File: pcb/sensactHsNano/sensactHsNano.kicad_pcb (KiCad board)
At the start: 2 copper layers, 90 x 58.5 mm, 130 parts, among them J1 PROG, J2 SensactBus, J3 CAN+24V, J4 HR911105A, J5 Audio, J6 1wire, Q1 BC817, SW1 TERM, SW2 Prog, SW3 Reset, U1 TAS5805M, U10 HT75xx-1-SOT89, U2 LAN8720A, U3 ESP32, U4 DS2482, U5 SN65HVD230, U6 EL817, U7 TPS5430DDA, U8 EL817, U9 LM393, X1 50MHz

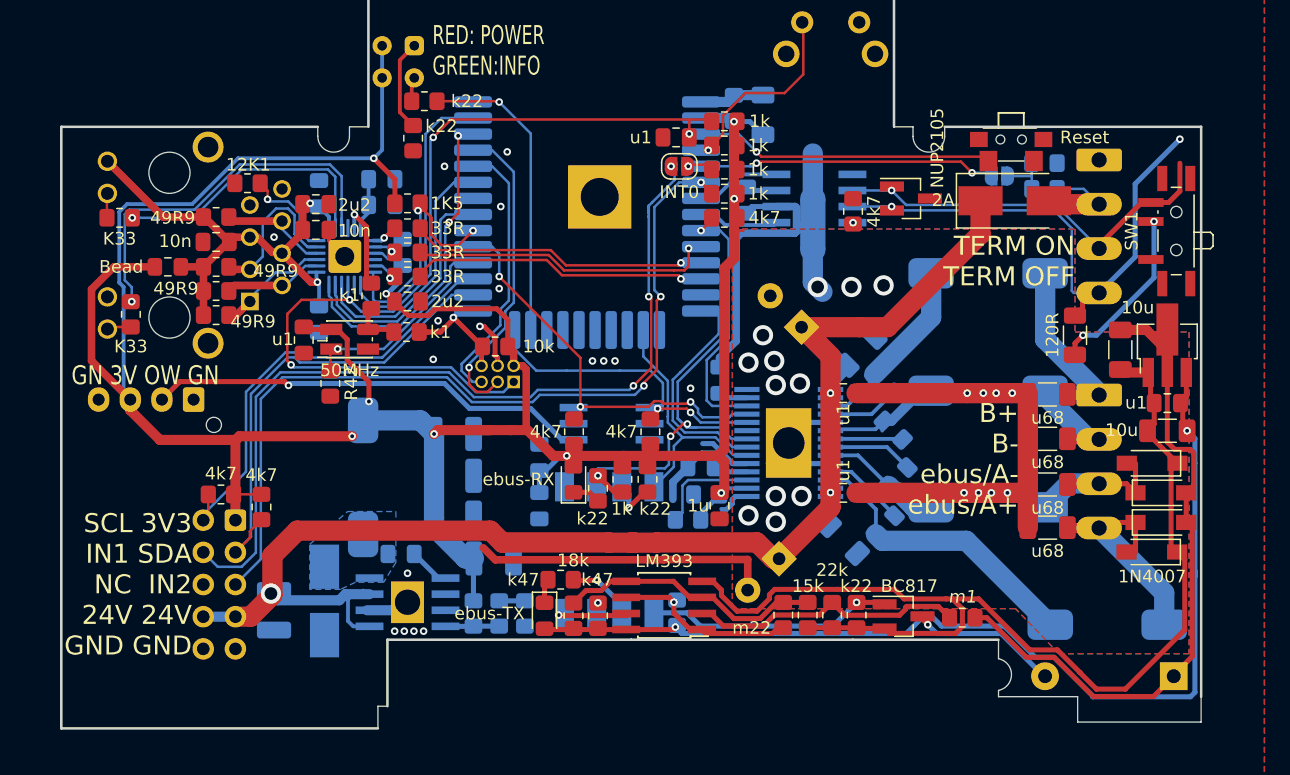
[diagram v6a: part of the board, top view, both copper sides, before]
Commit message: sensactHsNano for Reflow Soldering
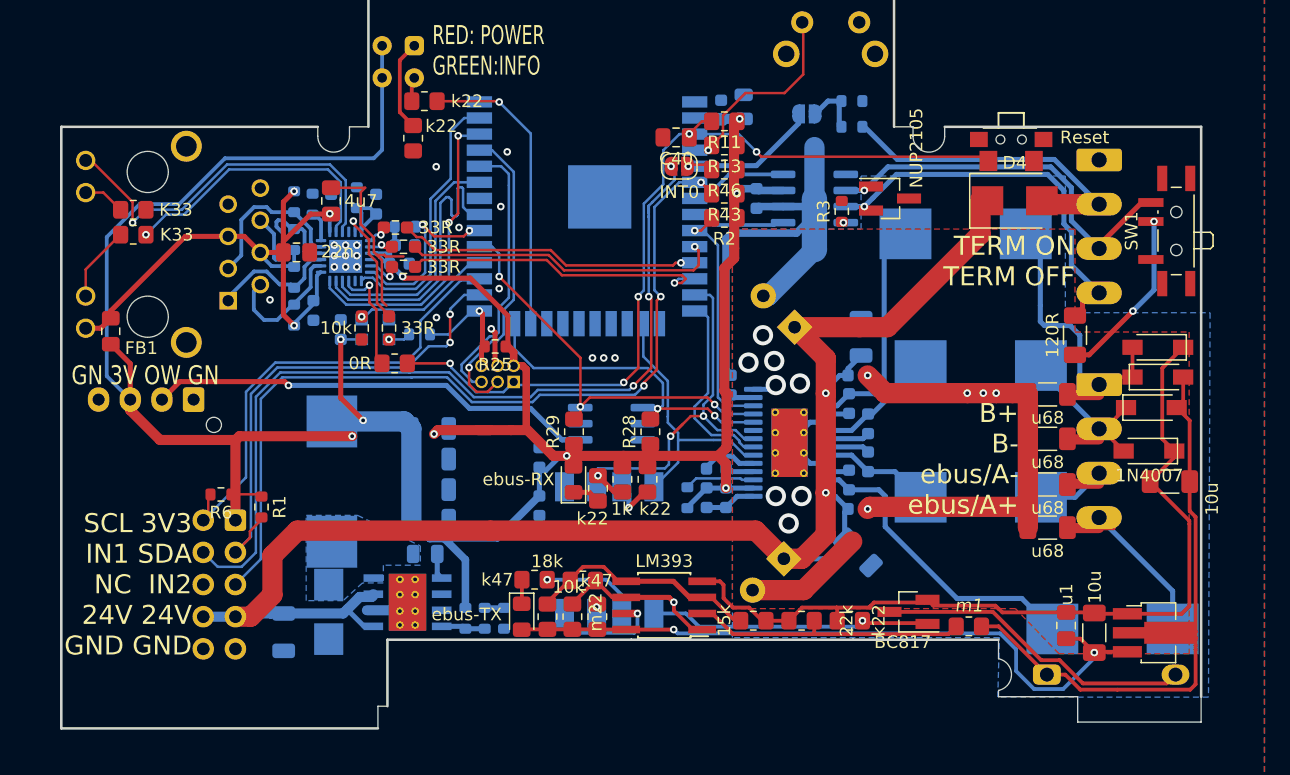
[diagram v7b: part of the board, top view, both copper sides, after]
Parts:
- removed C31: 10n, Capacitor_SMD:C_0805_2012Metric_Pad1.18x1.45mm_HandSolder
- added R47: 0R, Resistor_SMD:R_0805_2012Metric_Pad1.20x1.40mm_HandSolder, F.Cu at (131.3, 126.4)
- C10, C21, C26, C5: footprint Capacitor_SMD:C_0805_2012Metric_Pad1.18x1.45mm_HandSolder -> Capacitor_SMD:C_0603_1608Metric; moved to B.Cu
- C11, C12, C13, C14, C19, C20, C22, C25, C27, C28, C32, C4, C6, C7: footprint Capacitor_SMD:C_0805_2012Metric_Pad1.18x1.45mm_HandSolder -> Capacitor_SMD:C_0603_1608Metric
- C2: value 1u -> 4u7; footprint Capacitor_SMD:C_0805_2012Metric_Pad1.18x1.45mm_HandSolder -> Capacitor_SMD:C_0603_1608Metric; moved to B.Cu
- C23: value u1 -> n47; footprint Capacitor_SMD:C_0805_2012Metric_Pad1.18x1.45mm_HandSolder -> Capacitor_SMD:C_0603_1608Metric
- C24: value 2u2 -> 1u; footprint Capacitor_SMD:C_0805_2012Metric_Pad1.18x1.45mm_HandSolder -> Resistor_SMD:R_0603_1608Metric
- C29: value 2u2 -> 4u7
- C3, C9: footprint Capacitor_SMD:C_1206_3216Metric_Pad1.33x1.80mm_HandSolder -> Capacitor_SMD:C_1206_3216Metric
- C30: value 10n -> 22n
- C33: footprint Capacitor_SMD:C_1206_3216Metric_Pad1.33x1.80mm_HandSolder -> Capacitor_SMD:C_0805_2012Metric
- C34, C36, C37, C38, C39: footprint Capacitor_SMD:C_1210_3225Metric_Pad1.33x2.70mm_HandSolder -> Capacitor_SMD:C_1206_3216Metric
- C35: footprint Capacitor_SMD:C_0805_2012Metric_Pad1.18x1.45mm_HandSolder -> Capacitor_SMD:C_0805_2012Metric
- D2, D4: footprint Diode_SMD:D_SMB_Handsoldering -> Diode_SMD:D_SMB
- J4: footprint liebler_CONN:HANRUN_HR911105A -> liebler_CONN:RJ45_HANRUN_HR911105A
- L1, L2, L3, L4, L5: footprint liebler_PASSIVES:Inductor_CDRH104_handsolder -> liebler_PASSIVES:L_1040
- R1, R22, R23, R24, R25, R3, R4, R44, R45, R6: footprint Resistor_SMD:R_0805_2012Metric_Pad1.20x1.40mm_HandSolder -> Resistor_SMD:R_0603_1608Metric
- R10, R12, R42, R9: footprint Resistor_SMD:R_0805_2012Metric_Pad1.20x1.40mm_HandSolder -> Resistor_SMD:R_0603_1608Metric_Pad0.98x0.95mm_HandSolder
- R14: value k1 -> 33R; footprint Resistor_SMD:R_0805_2012Metric_Pad1.20x1.40mm_HandSolder -> Resistor_SMD:R_0603_1608Metric_Pad0.98x0.95mm_HandSolder
- R15, R16, R17, R18, R19, R5: footprint Resistor_SMD:R_0805_2012Metric_Pad1.20x1.40mm_HandSolder -> Resistor_SMD:R_0603_1608Metric; moved to B.Cu
- R35: moved to F.Cu
- R8: value k1 -> 33R; footprint Resistor_SMD:R_0805_2012Metric_Pad1.20x1.40mm_HandSolder -> Resistor_SMD:R_0603_1608Metric; moved to B.Cu
- U1: footprint sensact:TSSOP-28_4.4x9.7mm_Pitch0.65mm_pad_handsolder -> Package_SO:HTSSOP-28-1EP_4.4x9.7mm_P0.65mm_EP2.85x5.4mm_ThermalVias
- U2: footprint sensact:QFN-24-1EP_4x4mm_P0.5mm_EP2.6x2.6mm_handsolder -> Package_DFN_QFN:QFN-24-1EP_4x4mm_P0.5mm_EP2.6x2.6mm
- U3: footprint smopla:ESP32-WROOM-32_HANDSOLDER -> RF_Module:ESP32-WROOM-32
- U4, U5: footprint sensact:SOIC-8_3.9x4.9mm_Pitch1.27mm_handsolder -> Package_SO:SOIC-8_3.9x4.9mm_P1.27mm
- U7: footprint sensact:SOIC-8_3.9x4.9mm_Pitch1.27mm_pad_handsolder -> Package_SO:TI_SO-PowerPAD-8_ThermalVias
- X1: footprint Oscillator:Oscillator_SMD_EuroQuartz_XO32-4Pin_3.2x2.5mm_HandSoldering -> Oscillator:Oscillator_SMD_EuroQuartz_XO32-4Pin_3.2x2.5mm; moved to B.Cu
- moved U10 22.7 mm to (191.3, 147.7), turned to 0 degrees
- moved C43 19.3 mm to (184.3, 147.1), turned to 90 degrees
- moved C42 17.0 mm to (186.6, 147.7), turned to 90 degrees
- moved R36 16.1 mm to (146.2, 143.6), turned to 0 degrees
- moved R44 16.0 mm to (167.4, 107.7)
- moved R45 16.0 mm to (167.4, 105.7)
- moved JP2 16.0 mm to (163.9, 106.7)
- moved C41 11.1 mm to (192.5, 135.8), turned to 180 degrees
- moved D7 10.0 mm to (182.8, 151.0), turned to 0 degrees
- moved D9 9.17 mm to (191.6, 125.2)
- moved D8 9.15 mm to (191.6, 127.5)
- moved D11 9.10 mm to (191.1, 129.9)
- moved R35 8.27 mm to (145.4, 146.4)
- moved R20 8.26 mm to (110.7, 114.3), turned to 0 degrees
- moved R18 8.02 mm to (123.4, 113.7), turned to 270 degrees
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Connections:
- D10 pad 2: OUT_A+ -> OUT_B-
- D11 pad 1: OUT_A+ -> OUT_B-
- D8 pad 1: OUT_A- -> OUT_B+
- D9 pad 2: OUT_A- -> OUT_B+
- J4 pad 10: GND -> Net-(J4-Pad10)
- J4 pad 12: /eth/VDD2A -> /eth/LED1
- J4 pad 9: Net-(J4-Pad9) -> /eth/VDD2A
- R20 pad 1: Net-(J4-Pad9) -> Net-(J4-Pad11)
- R20 pad 2: /eth/LED1 -> GND
- R21 pad 2: Net-(J4-Pad11) -> Net-(J4-Pad10)
- U2 pad 15: EN -> Net-(R47-Pad2)
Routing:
- net EN: track 96.1 -> 67.4 mm
- net +5VA: track 81.4 -> 54.9 mm
- net GND1: track 85.6 -> 66.5 mm
- net Net-(D4-Pad2): track 7.95 -> 26.5 mm
- net GNDA: track 77.0 -> 60.5 mm, vias 20 -> 13
- net SENSOR_VN: track 26.3 -> 12.1 mm, vias 3 -> 1
- net Net-(D7-Pad2): track 11.8 -> 25.2 mm, vias 1 -> 0
- net CANH: track 44.1 -> 32.2 mm, vias 2 -> 1
- net Net-(R47-Pad2): track 0.00 -> 9.01 mm, vias 0 -> 1
- net /eth/VDD2A: track 40.0 -> 47.3 mm, vias 2 -> 3
- net OUT_B-: track 8.68 -> 15.0 mm
- net Net-(J4-Pad10): track 0.00 -> 6.00 mm
- net ETH_MDIO: track 19.7 -> 13.9 mm
- net Net-(R16-Pad2): track 8.12 -> 2.52 mm, vias 1 -> 0
- net ETH_TX0: track 19.1 -> 24.3 mm
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
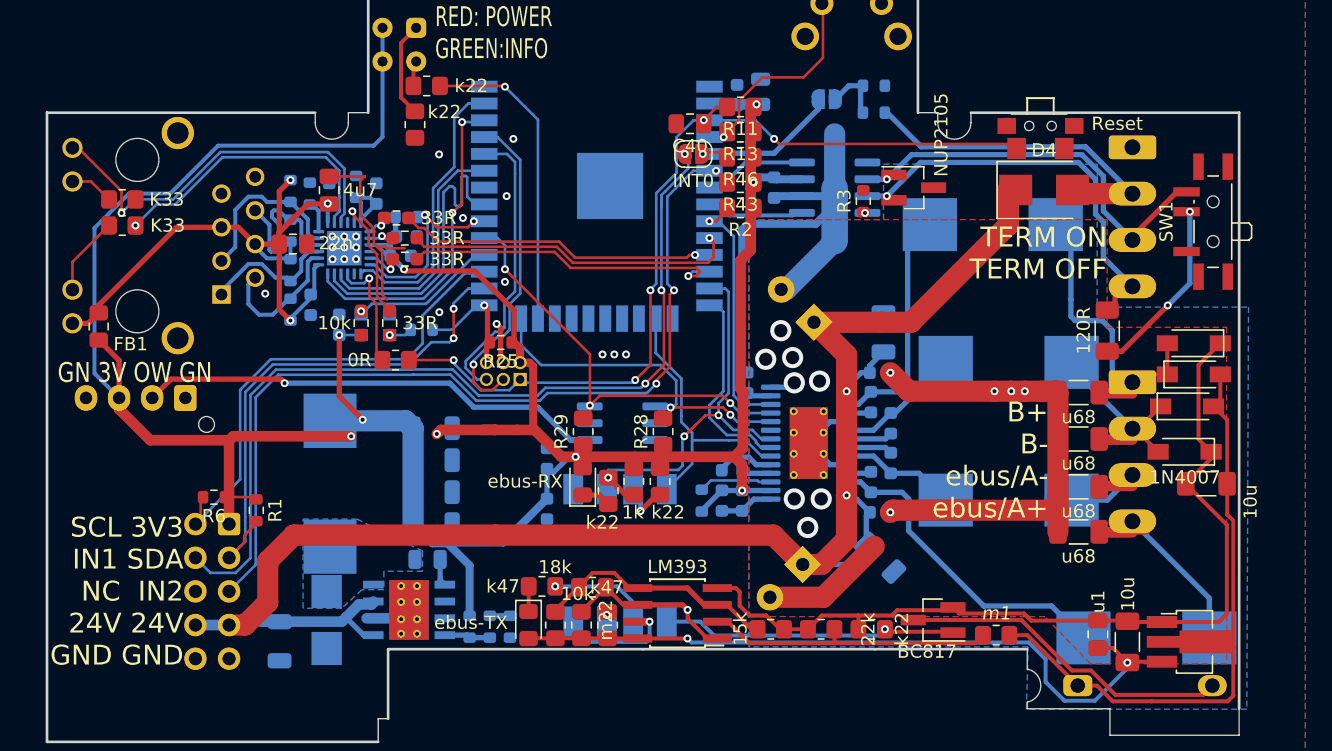
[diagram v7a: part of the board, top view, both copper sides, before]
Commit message: Updated pin mapping
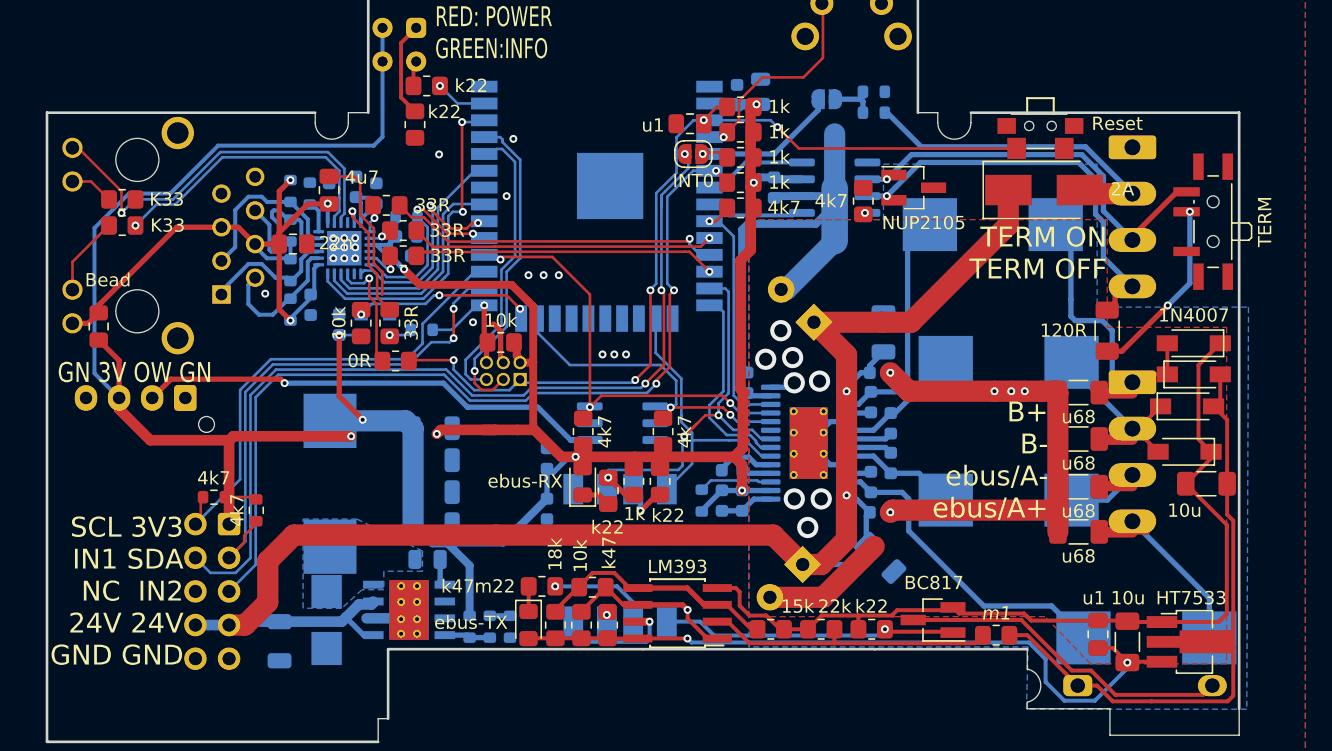
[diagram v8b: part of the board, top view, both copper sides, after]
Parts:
- C24: footprint Resistor_SMD:R_0603_1608Metric -> Capacitor_SMD:C_0603_1608Metric
- D4: footprint Diode_SMD:D_SMB -> Diode_SMD:D_SMB_Handsoldering
- R10, R12, R14, R42, R9: footprint Resistor_SMD:R_0603_1608Metric_Pad0.98x0.95mm_HandSolder -> Resistor_SMD:R_0805_2012Metric_Pad1.20x1.40mm_HandSolder
- R25, R3: footprint Resistor_SMD:R_0603_1608Metric -> Resistor_SMD:R_0805_2012Metric_Pad1.20x1.40mm_HandSolder
- U10: value HT75xx-1-SOT89 -> HT7533
- moved R10 1.22 mm to (130.6, 114.7)
- moved R9 0.59 mm to (131.9, 116.6)
- moved R45 0.45 mm to (167.4, 106.2)
- moved R12 0.28 mm to (131.9, 118.6)
- moved R47 0.06 mm to (131.3, 126.5)
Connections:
- U3 pad 23: Net-(R26-Pad2) -> SDA2
- U3 pad 24: SDA2 -> ETH_POWER
- U3 pad 28: ETH_POWER -> SCL2
- U3 pad 29: SCL2 -> ETH_MDIO
- U3 pad 30: ETH_MDIO -> ETH_MDC
- U3 pad 37: ETH_MDC -> Net-(R26-Pad2)
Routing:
- net Net-(R26-Pad2): track 24.0 -> 5.39 mm
- net ETH_MDC: track 22.6 -> 15.8 mm, vias 0 -> 2
- net ETH_TX0: track 24.3 -> 17.6 mm
- net GND: track 60.6 -> 57.3 mm
- net +3V3: track 226.3 -> 229.6 mm
- net ETH_POWER: track 11.2 -> 13.8 mm, vias 1 -> 3
- net ETH_RX0: track 24.9 -> 22.9 mm
- net ETH_MDIO: track 13.9 -> 15.6 mm
- net ETH_CRS: track 25.0 -> 23.3 mm
- net SCL2: track 32.8 -> 34.3 mm
- net ETH_RX1: track 24.5 -> 25.9 mm
- net SDA2: track 26.3 -> 25.0 mm
- net SUPPLY_MONITOR: track 4.36 -> 3.63 mm
- net PROG_TX: track 25.2 -> 24.5 mm
